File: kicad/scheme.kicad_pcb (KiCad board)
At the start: 2 copper layers, 40 x 100 mm, 46 parts, among them J1 reset, Q1 G1, SW1 SW_PUSH_6mm_H4.3mm, SW2 SW_PUSH_6mm_H4.3mm, SW3 SW_PUSH_6mm_H4.3mm, SW4 btn-start, SW5 SW_PUSH_6mm_H4.3mm, U1 COM-09032-103-530, U2 ESP-12E-no_pins, U3 PCA9306, U4 AP2112K-3.3, U5 ADS1015IDGS, U6 ME6211C18M5, U7 ICM-20948

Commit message: kicad-updates
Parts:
- removed ICM-conn1: AUX-ICM-no!, Connector_PinHeader_2.54mm:PinHeader_1x04_P2.54mm_Vertical
- added J2: Conn_01x04, Connector_PinSocket_2.54mm:PinSocket_1x04_P2.54mm_Vertical, B.Cu at (159.5, 51.9)
- U5, U7: moved to B.Cu
- moved C9 2.10 mm to (131.5, 92.0)
- moved C8 1.54 mm to (124.3, 104.2)
- moved U7 1.50 mm to (126.8, 94.8), turned to -90 degrees
- moved C3 0.79 mm to (124.3, 108.0)
- moved R12 0.59 mm to (124.3, 100.4), turned to 180 degrees
- moved C2 0.17 mm to (124.3, 111.8)
- turned R11 to 0 degrees
- turned U5 to 180 degrees
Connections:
- U7 pad 11: Net-(ICM-conn1-Pin_1) -> unconnected-(U7-FSYNC-Pad11)
- U7 pad 12: Net-(ICM-conn1-Pin_2) -> unconnected-(U7-INT1-Pad12)
- U7 pad 21: /aux-da -> unconnected-(U7-AUX_DA-Pad21)
- U7 pad 7: /aux_cl -> unconnected-(U7-AUX_CL-Pad7)
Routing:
- net GND: track 370.7 -> 0.00 mm, vias 4 -> 0
- net +3.3V: track 280.6 -> 0.00 mm, vias 3 -> 0
- net +1.8V: track 96.5 -> 0.00 mm, vias 5 -> 0
- net /SCL: track 94.8 -> 0.00 mm, vias 5 -> 0
- net /btn_103-530: track 94.8 -> 0.00 mm, vias 2 -> 0
- net +4.2V: track 92.9 -> 0.00 mm, vias 2 -> 0
- net /SDA: track 89.5 -> 0.00 mm, vias 3 -> 0
- net Net-(D1-K): track 88.3 -> 0.00 mm
- net Net-(D1-A): track 76.7 -> 0.00 mm
- net Net-(J1-Pin_1): track 68.8 -> 0.00 mm, vias 1 -> 0
- net /btnA: track 66.6 -> 0.00 mm, vias 3 -> 0
- net Net-(U7-SDO/AD0): track 65.5 -> 0.00 mm, vias 2 -> 0
- net Net-(TP4056-module1-b+): track 62.1 -> 0.00 mm
- net /SDA_1.8: track 55.7 -> 0.00 mm, vias 3 -> 0
- net /SCL_1.8: track 52.7 -> 0.00 mm, vias 3 -> 0
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- added copper zone on B.Cu, net GND
- added copper zone on F.Cu, net GND

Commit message: changes in scheme
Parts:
- added R16: R-100, Resistor_SMD:R_0805_2012Metric, F.Cu at (131.9, 98.5)
- added R17: 4k7, Resistor_SMD:R_0805_2012Metric_Pad1.20x1.40mm_HandSolder, F.Cu at (158.4, 123.2)
- added R18: 1k, Resistor_SMD:R_0805_2012Metric_Pad1.20x1.40mm_HandSolder, F.Cu at (143.1, 97.0)
- added S1: SLW-883935-2A-D, module-custom-for-esp8266:SW_SLW-883935-2A-D, B.Cu at (126.2, 141.6)
- U5, U7: moved to F.Cu
- moved C1 51.8 mm to (159.1, 90.4)
- moved C3 43.3 mm to (158.9, 82.0), turned to 0 degrees
- moved J1 38.7 mm to (159.7, 128.3), turned to -90 degrees
- moved R13 34.9 mm to (131.9, 94.1), turned to 180 degrees
- moved R6 19.0 mm to (155.9, 141.4), turned to -90 degrees
- moved R7 16.7 mm to (152.9, 141.4), turned to -90 degrees
- moved R8 15.3 mm to (149.8, 141.4), turned to -90 degrees
- moved R14 15.0 mm to (146.8, 141.4), turned to 90 degrees
- moved C9 11.7 mm to (124.4, 101.3), turned to 180 degrees
- moved R12 9.76 mm to (124.6, 90.6)
- moved U4 2.88 mm to (159.0, 86.7)
- moved U6 2.48 mm to (153.4, 126.6)
- moved C10 1.94 mm to (129.8, 119.8), turned to 180 degrees
- moved R15 1.92 mm to (124.6, 88.1)
- moved C7 1.73 mm to (124.4, 116.1)
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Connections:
- net Net-(TP4056-module1-b+) renamed /bt+
- R6 pad 1: Net-(U2-GPIO15) -> Net-(SW4-C)
- SW4 pad 1: GND -> Net-(SW4-C)
- TP4056-module1 pad 3: +4.2V -> Net-(TP4056-module1-out+)
- U2 pad 16: Net-(U2-GPIO15) -> Net-(SW4-C)
- U2 pad 2: Net-(SW4-D) -> Net-(U2-ADC)

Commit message: added Readme
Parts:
- C1: renamed from C5; footprint Capacitor_SMD:C_0805_2012Metric -> Resistor_SMD:R_0805_2012Metric_Pad1.20x1.40mm_HandSolder
- C2: renamed from C9; footprint Capacitor_SMD:C_0805_2012Metric -> Resistor_SMD:R_0805_2012Metric_Pad1.20x1.40mm_HandSolder
- C3: renamed from C8; footprint Capacitor_SMD:C_0805_2012Metric -> Resistor_SMD:R_0805_2012Metric_Pad1.20x1.40mm_HandSolder
- C4: renamed from C7; footprint Capacitor_THT:CP_Radial_D10.0mm_P3.50mm -> Resistor_SMD:R_0805_2012Metric_Pad1.20x1.40mm_HandSolder; moved to F.Cu
- C5: renamed from C2; footprint Capacitor_SMD:C_0805_2012Metric -> Resistor_SMD:R_0805_2012Metric_Pad1.20x1.40mm_HandSolder
- C6: renamed from C4; footprint Capacitor_SMD:C_0805_2012Metric -> Resistor_SMD:R_0805_2012Metric_Pad1.20x1.40mm_HandSolder
- C7: renamed from C10; footprint Capacitor_SMD:C_0805_2012Metric -> Resistor_SMD:R_0805_2012Metric_Pad1.20x1.40mm_HandSolder
- C8: renamed from C3; footprint Capacitor_SMD:C_0805_2012Metric -> Resistor_SMD:R_0805_2012Metric_Pad1.20x1.40mm_HandSolder
- C9: renamed from C1; footprint Capacitor_SMD:C_0805_2012Metric -> Resistor_SMD:R_0805_2012Metric_Pad1.20x1.40mm_HandSolder
- R1: renamed from R11; footprint Resistor_SMD:R_0805_2012Metric -> Resistor_SMD:R_0805_2012Metric_Pad1.20x1.40mm_HandSolder
- R12: renamed from R14; footprint Resistor_SMD:R_0805_2012Metric -> Resistor_SMD:R_0805_2012Metric_Pad1.20x1.40mm_HandSolder
- R13: renamed from R8; footprint Resistor_SMD:R_0805_2012Metric -> Resistor_SMD:R_0805_2012Metric_Pad1.20x1.40mm_HandSolder
- R14: renamed from R4; footprint Resistor_SMD:R_0805_2012Metric -> Resistor_SMD:R_0805_2012Metric_Pad1.20x1.40mm_HandSolder
- R15: renamed from R5; footprint Resistor_SMD:R_0805_2012Metric -> Resistor_SMD:R_0805_2012Metric_Pad1.20x1.40mm_HandSolder
- R16: renamed from R7; footprint Resistor_SMD:R_0805_2012Metric -> Resistor_SMD:R_0805_2012Metric_Pad1.20x1.40mm_HandSolder
- R18: renamed from R6; footprint Resistor_SMD:R_0805_2012Metric -> Resistor_SMD:R_0805_2012Metric_Pad1.20x1.40mm_HandSolder
- R2: renamed from R15; footprint Resistor_SMD:R_0805_2012Metric -> Resistor_SMD:R_0805_2012Metric_Pad1.20x1.40mm_HandSolder
- R4: renamed from R13; footprint Resistor_SMD:R_0805_2012Metric -> Resistor_SMD:R_0805_2012Metric_Pad1.20x1.40mm_HandSolder
- R8: renamed from R12; footprint Resistor_SMD:R_0805_2012Metric -> Resistor_SMD:R_0805_2012Metric_Pad1.20x1.40mm_HandSolder
- R9: renamed from R16; footprint Resistor_SMD:R_0805_2012Metric -> Resistor_SMD:R_0805_2012Metric_Pad1.20x1.40mm_HandSolder
- S1: footprint module-custom-for-esp8266:SW_SLW-883935-2A-D -> module-custom-for-esp8266:SW_OS102011MS2QN1_slideSwitch
- moved C9 43.3 mm to (152.8, 133.3)
- moved C8 43.2 mm to (152.8, 124.8)
- moved U7 42.8 mm to (152.4, 129.1)
- moved C5 41.1 mm to (159.1, 89.8)
- moved S1 32.7 mm to (158.8, 138.1), turned to 90 degrees
- moved C1 28.4 mm to (150.2, 69.5), turned to 180 degrees
- moved U6 28.3 mm to (125.3, 122.9)
- moved R10 28.0 mm to (131.1, 117.3)
- moved R1 27.1 mm to (129.6, 76.4)
- moved R12 22.2 mm to (134.3, 123.0)
- moved R13 22.2 mm to (137.3, 123.0)
- moved R16 22.2 mm to (140.4, 123.0)
- moved R18 22.2 mm to (143.4, 123.0)
- moved R17 21.5 mm to (147.8, 118.0)
- moved prog1 17.5 mm to (159.8, 124.5)
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- renumbered D2 to D1, D1 to D2, D4 to D3, D3 to D4, R17 to R10, R10 to R11, R18 to R17, R2 to R3, R9 to R5, R3 to R6, R1 to R7, SW4 to SW2, SW2 to SW4, TP4056-module1 to TP1, U5 to U2, U7 to U3, U2 to U4, U3 to U5, U4 to U7
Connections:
- J2 pad 1: +4.2V -> +3.3V
- R18 pad 1: Net-(SW4-C) -> GND
- R18 pad 2: GND -> Net-(SW4-C)
- S1 pad 1: unconnected-(S1-Pad1) -> Net-(TP4056-module1-out+)
- S1 pad 2: Net-(TP4056-module1-out+) -> +4.2V
- S1 pad 3: +4.2V -> unconnected-(S1-Pad3)
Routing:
- net GND: track 0.00 -> 418.2 mm, vias 0 -> 3
- net +3.3V: track 0.00 -> 236.5 mm, vias 0 -> 4
- net /SCL: track 0.00 -> 128.2 mm, vias 0 -> 5
- net /SDA: track 0.00 -> 126.1 mm, vias 0 -> 5
- net Net-(D1-A): track 0.00 -> 106.4 mm, vias 0 -> 1
- net +1.8V: track 0.00 -> 100.3 mm, vias 0 -> 4
- net Net-(D1-K): track 0.00 -> 91.4 mm
- net /btn_103-530: track 0.00 -> 78.5 mm, vias 0 -> 2
- net /bt+: track 0.00 -> 76.3 mm, vias 0 -> 1
- net /SCL_1.8: track 0.00 -> 53.6 mm, vias 0 -> 3
- net /btnA: track 0.00 -> 52.3 mm, vias 0 -> 1
- net Net-(SW4-C): track 0.00 -> 51.5 mm
- net +4.2V: track 0.00 -> 50.0 mm, vias 0 -> 2
- net /SDA_1.8: track 0.00 -> 49.5 mm, vias 0 -> 3
- net Net-(J1-Pin_1): track 0.00 -> 38.8 mm, vias 0 -> 1
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
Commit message: udpate in scheme
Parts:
- removed C6: 0.1uF, Resistor_SMD:R_0805_2012Metric_Pad1.20x1.40mm_HandSolder
- added C10: 10uF, Resistor_SMD:R_0805_2012Metric_Pad1.20x1.40mm_HandSolder, F.Cu at (129.6, 71.8)
- added TP2: SDA_1.8, TestPoint:TestPoint_Pad_1.0x1.0mm, F.Cu at (146.2, 130.6)
- added TP3: SCL_1.8, TestPoint:TestPoint_Pad_1.0x1.0mm, F.Cu at (146.2, 132.7)
- added TP4: CS, TestPoint:TestPoint_Pad_1.0x1.0mm, F.Cu at (146.2, 134.8)
- added TP4056-module1: ~, module-custom-for-esp8266:TP4056-short, F.Cu at (121.7, 143.3)
- added TP5: 1.8V, TestPoint:TestPoint_Pad_1.0x1.0mm, F.Cu at (146.2, 137.0)
- C1, C7: value 10uF -> 0.1uF
- C4: value C_Electrolitic_3.3V -> 0.1uF
- C5: value 0.1uF -> 10uF
- R1: value R-1k -> 4k7
- R11: value 4k7 -> R-1k
- R13, R16: value R-10k -> R-100
- R14, R15: value R-100 -> R-10k
- R17: value 1k -> 4k7
- R18: value R-10k -> 1k
- R2: value R-10k -> 4k7
- R5: value 4k7 -> R-100
- R6, R7: value 4k7 -> R-10k
- R9: value R-100 -> 4k7
- SW2: value btn-start -> SW_PUSH_6mm_H4.3mm
- SW4: value SW_PUSH_6mm_H4.3mm -> btnB
- TP1: value ~ -> SDO; footprint module-custom-for-esp8266:TP4056-Module -> TestPoint:TestPoint_Pad_1.0x1.0mm
- U2: value ADS1015IDGS -> ESP-12E-no_pins; footprint Package_SO:VSSOP-10_3x3mm_P0.5mm -> module-custom-for-esp8266:ESP-12E_no_pins
- U3: value ICM-20948 -> PCA9306; footprint Sensor_Motion:InvenSense_QFN-24_3x3mm_P0.4mm -> Package_SO:MSOP-8_3x3mm_P0.65mm
- U4: value ESP-12E-no_pins -> AP2112K-3.3; footprint module-custom-for-esp8266:ESP-12E_no_pins -> module-custom-for-esp8266:SOT25
- U5: value PCA9306 -> ADS1015IDGS; footprint Package_SO:MSOP-8_3x3mm_P0.65mm -> Package_SO:VSSOP-10_3x3mm_P0.5mm
- U7: value AP2112K-3.3 -> ICM-20948; footprint module-custom-for-esp8266:SOT25 -> Sensor_Motion:InvenSense_QFN-24_3x3mm_P0.4mm
- moved C1 50.1 mm to (131.9, 116.1)
- moved R16 44.5 mm to (159.6, 82.8)
- moved U2 39.5 mm to (149.3, 105.7), turned to -90 degrees
- moved R12 38.7 mm to (159.1, 93.3), turned to 180 degrees
- moved R4 35.8 mm to (154.7, 119.1), turned to 0 degrees
- moved TP1 28.7 mm to (146.2, 128.5)
- moved R5 26.0 mm to (154.7, 116.9), turned to 0 degrees
- moved U4 23.3 mm to (133.5, 122.8)
- moved C3 13.8 mm to (131.9, 118.3)
- moved R11 13.7 mm to (131.0, 100.8)
- moved C9 6.64 mm to (151.7, 139.9)
- moved R14 5.65 mm to (155.1, 125.6)
- moved R15 5.30 mm to (155.0, 122.8)
- moved R10 5.29 mm to (131.0, 112.0)
- moved R6 5.28 mm to (131.0, 106.4), turned to 0 degrees
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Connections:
- BT1 pad -: Net-(TP4056-module1-b-) -> GND
- C1 pad 1: +3.3V -> +4.2V
- C2 pad 1: Net-(U7-REGOUT) -> +1.8V
- C5 pad 1: +1.8V -> +3.3V
- C9 pad 1: +4.2V -> Net-(U7-REGOUT)
- R1 pad 1: Net-(Q1-B) -> +3.3V
- R1 pad 2: /led-output -> Net-(U2-EN)
- R10 pad 1: /bt+ -> +3.3V
- R10 pad 2: Net-(U2-ADC) -> /SCL
- R11 pad 1: +3.3V -> Net-(Q1-B)
- R11 pad 2: /SCL -> /led-output
- R12 pad 1: Net-(U7-SDO/AD0) -> +3.3V
- R12 pad 2: GND -> Net-(U5-ALERT/RDY)
- R13 pad 1: /btn_103-530 -> Net-(D1-A)
- R14 pad 1: /tx -> Net-(U7-SDO/AD0)
- R14 pad 2: /tx-out -> GND
- R15 pad 1: /rx -> +3.3V
- R15 pad 2: /rx-out -> Net-(U7-~{CS})
- R16 pad 1: /btnA -> Net-(SW4-D)
- R17 pad 1: Net-(U2-ADC) -> /bt+
- R17 pad 2: GND -> Net-(U2-ADC)
- R18 pad 1: GND -> Net-(U2-ADC)
- R18 pad 2: Net-(SW4-C) -> GND
- R2 pad 1: +3.3V -> +1.8V
- R2 pad 2: Net-(U7-~{CS}) -> /SCL_1.8
- R3 pad 2: /SCL_1.8 -> /SDA_1.8
- R4 pad 1: Net-(D1-A) -> /tx
- R4 pad 2: +3.3V -> /tx-out
- R5 pad 1: +3.3V -> /rx
- R5 pad 2: /SDA -> /rx-out
- R6 pad 1: +1.8V -> GND
- R6 pad 2: /SDA_1.8 -> Net-(SW4-C)
- R7 pad 1: +3.3V -> /btnA
- R7 pad 2: Net-(U2-EN) -> +3.3V
- R8 pad 1: +3.3V -> /btn_103-530
- R8 pad 2: Net-(U5-ALERT/RDY) -> +3.3V
- R9 pad 1: Net-(SW4-D) -> +3.3V
- R9 pad 2: +3.3V -> /SDA
- S1 pad 1: Net-(TP4056-module1-out+) -> /bt+
- S1 pad 3: unconnected-(S1-Pad3) -> +5C
- SW1 pad 2: /btnX -> /btnY
- SW2 pad 1: Net-(SW4-C) -> GND
- SW2 pad 2: Net-(SW4-D) -> /btnA
- SW3 pad 2: /btnA -> /btnX
- SW4 pad 1: GND -> Net-(SW4-C)
- SW4 pad 2: /btnY -> Net-(SW4-D)
- SW5 pad 2: /btnB -> /btn-trigger
- TP1 pad 1: +5C -> Net-(U7-SDO/AD0)
- U2 pad 1: GND -> Net-(J1-Pin_1)
- U2 pad 2: Net-(U5-ALERT/RDY) -> Net-(U2-ADC)
- U2 pad 3: GND -> Net-(U2-EN)
- U2 pad 4: /analog0 -> /btn-trigger
- U2 pad 5: /analog1 -> /btnX
- U2 pad 6: unconnected-(U5-AIN2-Pad6) -> /led-output
- U2 pad 7: unconnected-(U5-AIN3-Pad7) -> /btnY
- U3 pad 1: unconnected-(U7-NC-Pad1) -> GND
- U3 pad 2: unconnected-(U7-NC-Pad2) -> +1.8V
- U3 pad 3: unconnected-(U7-NC-Pad3) -> /SCL_1.8
- U3 pad 4: unconnected-(U7-NC-Pad4) (its old number) -> /SDA_1.8
- U3 pad 5: unconnected-(U7-NC-Pad5) -> /SDA
- U3 pad 6: unconnected-(U7-NC-Pad6) -> /SCL
- U3 pad 7: unconnected-(U7-AUX_CL-Pad7) -> +3.3V
- U3 pad 8: +1.8V -> +3.3V
- U4 pad 1: Net-(J1-Pin_1) -> +4.2V
- U4 pad 2: Net-(U2-ADC) -> GND
- U4 pad 3: Net-(U2-EN) -> +4.2V
- U4 pad 4: /btnB -> unconnected-(U4-NC-Pad4)
- U4 pad 5: /btnX -> +3.3V
- U5 pad 2: +1.8V -> Net-(U5-ALERT/RDY)
- U5 pad 3: /SCL_1.8 -> GND
- U5 pad 4: /SDA_1.8 -> /analog0
- U5 pad 5: /SDA -> /analog1
- U5 pad 6: /SCL -> unconnected-(U5-AIN2-Pad6)
- U5 pad 7: +3.3V -> unconnected-(U5-AIN3-Pad7)
- U7 pad 1: +4.2V -> unconnected-(U7-NC-Pad1)
- U7 pad 2: GND -> unconnected-(U7-NC-Pad2)
- U7 pad 3: +4.2V -> unconnected-(U7-NC-Pad3)
- U7 pad 5: +3.3V -> unconnected-(U7-NC-Pad5)
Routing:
- net /btn-trigger: track 0.00 -> 41.3 mm, vias 0 -> 1
- net +3.3V: track 236.5 -> 276.3 mm, vias 4 -> 10
- net /btnB: track 37.9 -> 0.00 mm, vias 1 -> 0
- net /SDA_1.8: track 49.5 -> 85.5 mm, vias 3 -> 6
- net /analog0: track 20.4 -> 51.8 mm, vias 0 -> 1
- net /btn_103-530: track 78.5 -> 107.4 mm, vias 2 -> 3
- net /SCL: track 128.2 -> 99.5 mm, vias 5 -> 3
- net /SCL_1.8: track 53.6 -> 78.2 mm, vias 3 -> 4
- net Net-(D1-A): track 106.4 -> 130.7 mm
- net Net-(Q1-B): track 9.01 -> 31.9 mm
- net /analog1: track 31.2 -> 51.7 mm
- net Net-(TP4056-module1-out+): track 17.6 -> 0.00 mm
- net /led-output: track 29.9 -> 13.2 mm
- net +5C: track 37.1 -> 50.4 mm
- net /SDA: track 126.1 -> 113.3 mm, vias 5 -> 3
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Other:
- board text added: "3.3V GPIO13 GPIO12 GPIO14 GPIO16 EN ADC RST"
- board text added: "3.3V x"
- board text added: "4.2V GND 4.2V"
- board text added: "GND ALERT GND analog0 analog1"
- board text added: "GND GPIO15 GPIO2 GPIO0 GPIO4/SDA GPIO5/SCL GPIO3/RXD GPIO1/TXD"
- board text added: "GND x x x x 3.3V"
- board text added: "RST GND"
- board text added: "RX TX GND +5V"
- board text added: "SCL SDA 3.3V x x"
- board text added: "SDA SCL 1.8V GND"
- board text added: "SDA SCL 3.3V 3.3V"
- board text added: "SDA SCL GND 3.3V"
- board text added: "USB BT"
- board text added: "aux_CL 1.8V SD0 REGOUT FSYNC INT1"
- board text added: "sda scl cs nc GND x"
- board text added: "x 1.8V"

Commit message: update
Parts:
- added J3: AIN2-3, Connector_PinHeader_2.54mm:PinHeader_2x01_P2.54mm_Vertical, F.Cu at (149.8, 76.8)
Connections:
- BT1 pad -: GND -> unconnected-(BT1-Pad-)
- U5 pad 6: unconnected-(U5-AIN2-Pad6) -> Net-(J3-Pin_1)
- U5 pad 7: unconnected-(U5-AIN3-Pad7) -> Net-(J3-Pin_2)
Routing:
- net +1.8V: track 106.2 -> 86.7 mm
- net Net-(J3-Pin_1): track 0.00 -> 17.4 mm
- net /SCL: track 99.5 -> 116.6 mm, vias 3 -> 4
- net Net-(J3-Pin_2): track 0.00 -> 15.8 mm
- net GND: track 427.9 -> 412.2 mm
- net /SDA_1.8: track 85.5 -> 71.3 mm, vias 6 -> 2
- net /SCL_1.8: track 78.2 -> 86.9 mm, vias 4 -> 2
- net Net-(Q1-B): track 31.9 -> 38.5 mm
- net /SDA: track 113.3 -> 106.8 mm, vias 3 -> 5
- net /bt+: track 82.6 -> 76.7 mm, vias 0 -> 2
- net /btn-trigger: track 41.3 -> 35.6 mm
- net /analog0: track 51.8 -> 46.9 mm, vias 1 -> 2
- net Net-(U7-~{CS}): track 27.1 -> 22.2 mm
- net Net-(U7-SDO/AD0): track 27.8 -> 23.7 mm
- net Net-(SW4-C): track 60.1 -> 56.6 mm
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- removed copper zone on B.Cu, net GND
- removed copper zone on F.Cu, net GND

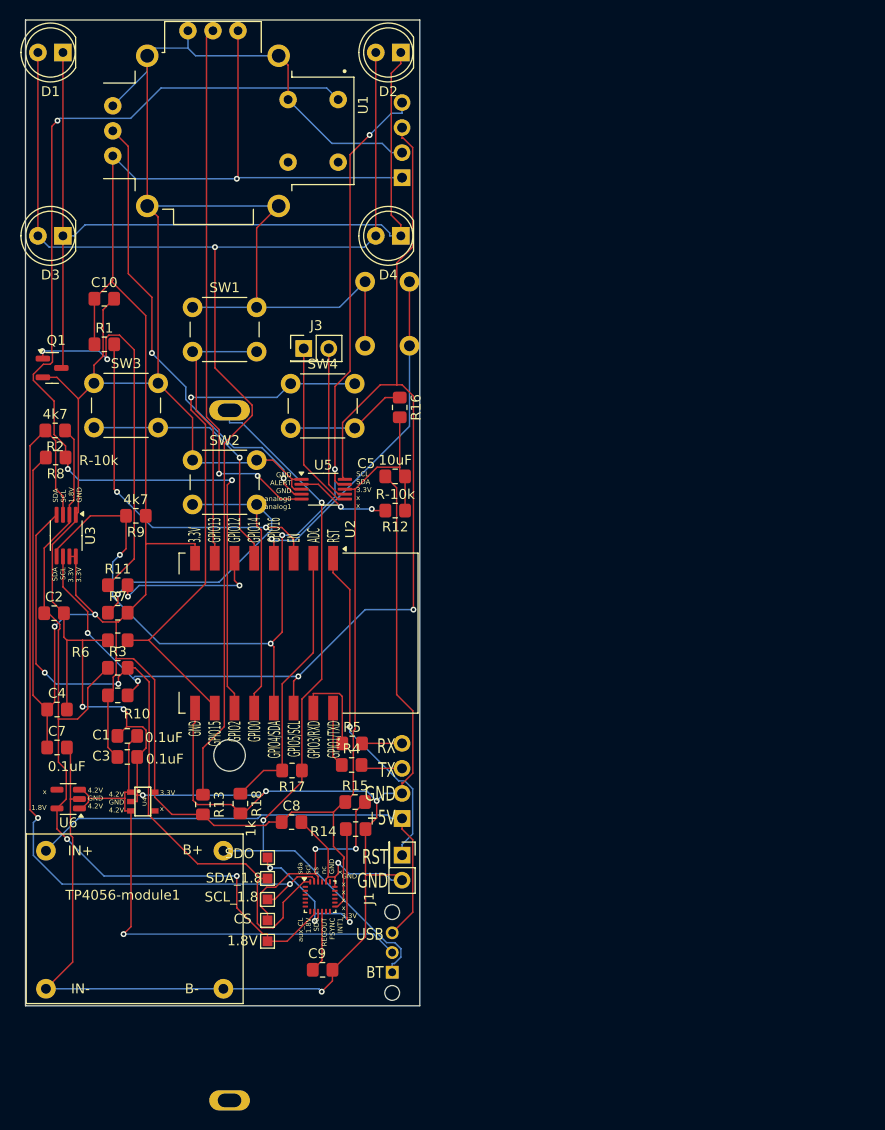
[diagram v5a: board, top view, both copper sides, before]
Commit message: Gyro mouse filter
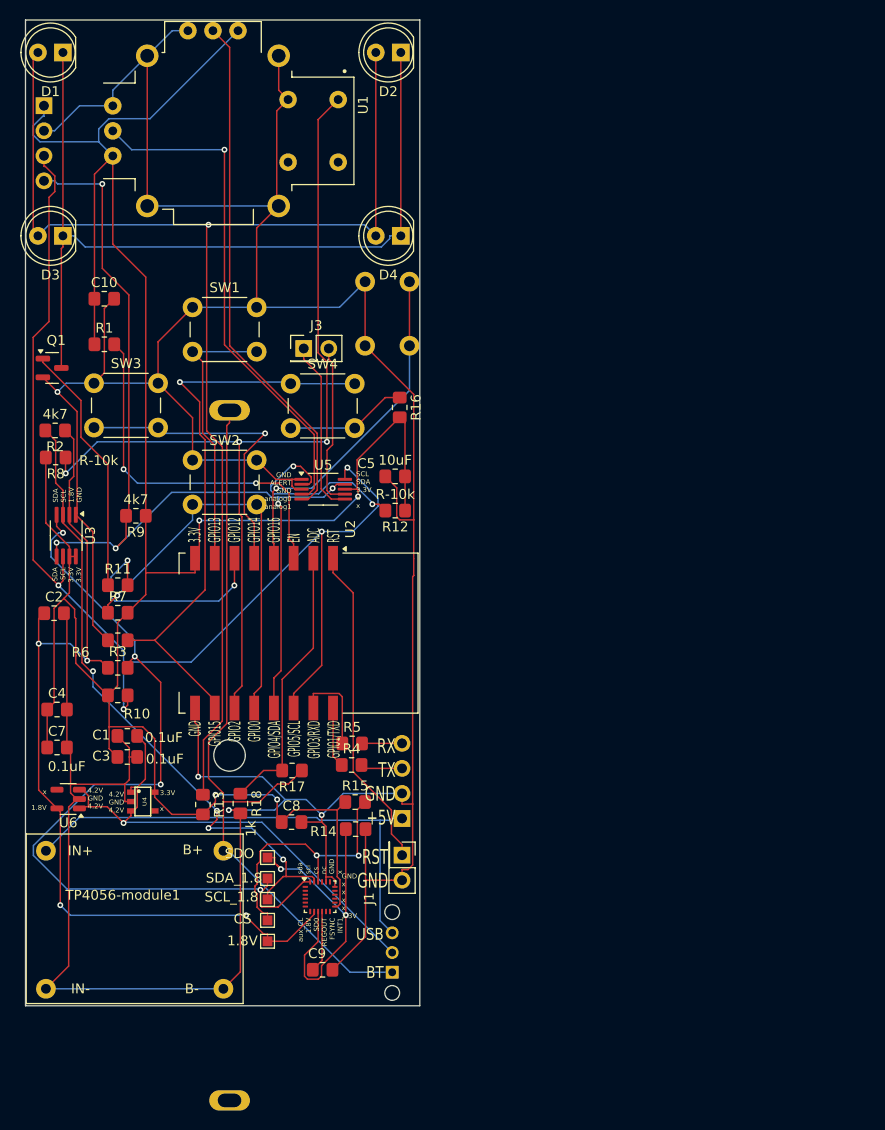
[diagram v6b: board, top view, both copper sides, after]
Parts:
- moved J2 37.1 mm to (123.5, 52.2), turned to 180 degrees
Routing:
- net +3.3V: track 275.3 -> 254.8 mm, vias 3 -> 4
- net /SCL_1.8: track 86.9 -> 67.0 mm, vias 2 -> 4
- net /btn_103-530: track 109.3 -> 92.8 mm
- net Net-(U7-SDO/AD0): track 23.7 -> 38.2 mm, vias 3 -> 2
- net /SDA_1.8: track 71.3 -> 85.1 mm, vias 2 -> 4
- net Net-(Q1-B): track 38.5 -> 25.7 mm, vias 2 -> 0
- net /led-output: track 15.9 -> 28.4 mm
- net Net-(U5-ALERT/RDY): track 9.61 -> 20.9 mm
- net /btnA: track 51.4 -> 42.2 mm
- net /SCL: track 116.6 -> 125.0 mm
- net /SDA: track 106.8 -> 100.5 mm
- net +1.8V: track 86.7 -> 92.6 mm, vias 2 -> 4
- net GND: track 412.2 -> 406.9 mm, vias 7 -> 4
- net Net-(U7-~{CS}): track 22.2 -> 27.3 mm
- net +4.2V: track 56.8 -> 51.8 mm
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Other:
- board text added: "3.3V GND SCL SDA"
- board text removed: "SDA SCL GND 3.3V"
